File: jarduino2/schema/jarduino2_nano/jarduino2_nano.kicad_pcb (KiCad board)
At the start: 2 copper layers, 118 x 95 mm, 38 parts, among them J1 Power, J2 Interface, J3 Pompe 1, J4 Pompe 2, Q1 Q_NPN_BCE, Q2 Q_NPN_BCE, U1 RFB-0505S, U2 RtcArduino

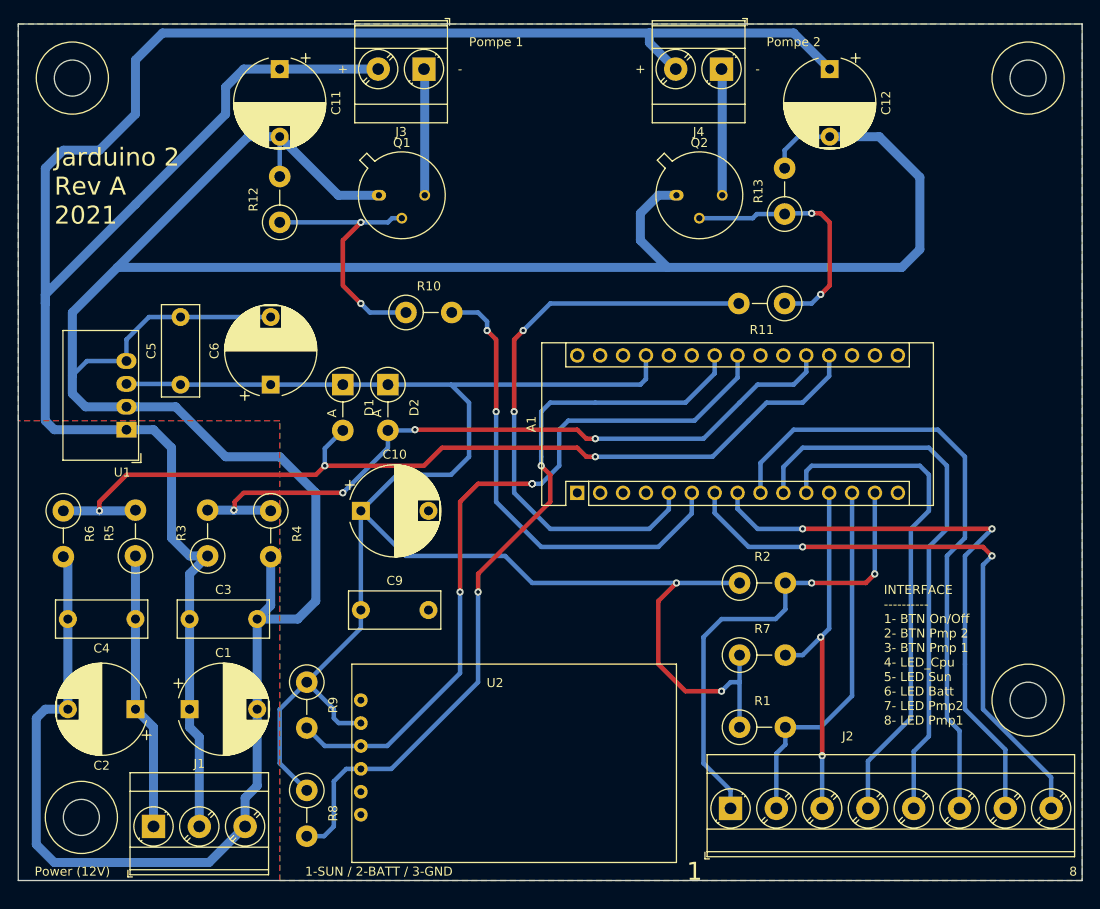
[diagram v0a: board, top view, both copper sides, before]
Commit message: Ajout capteur de temp et hum + ext serie
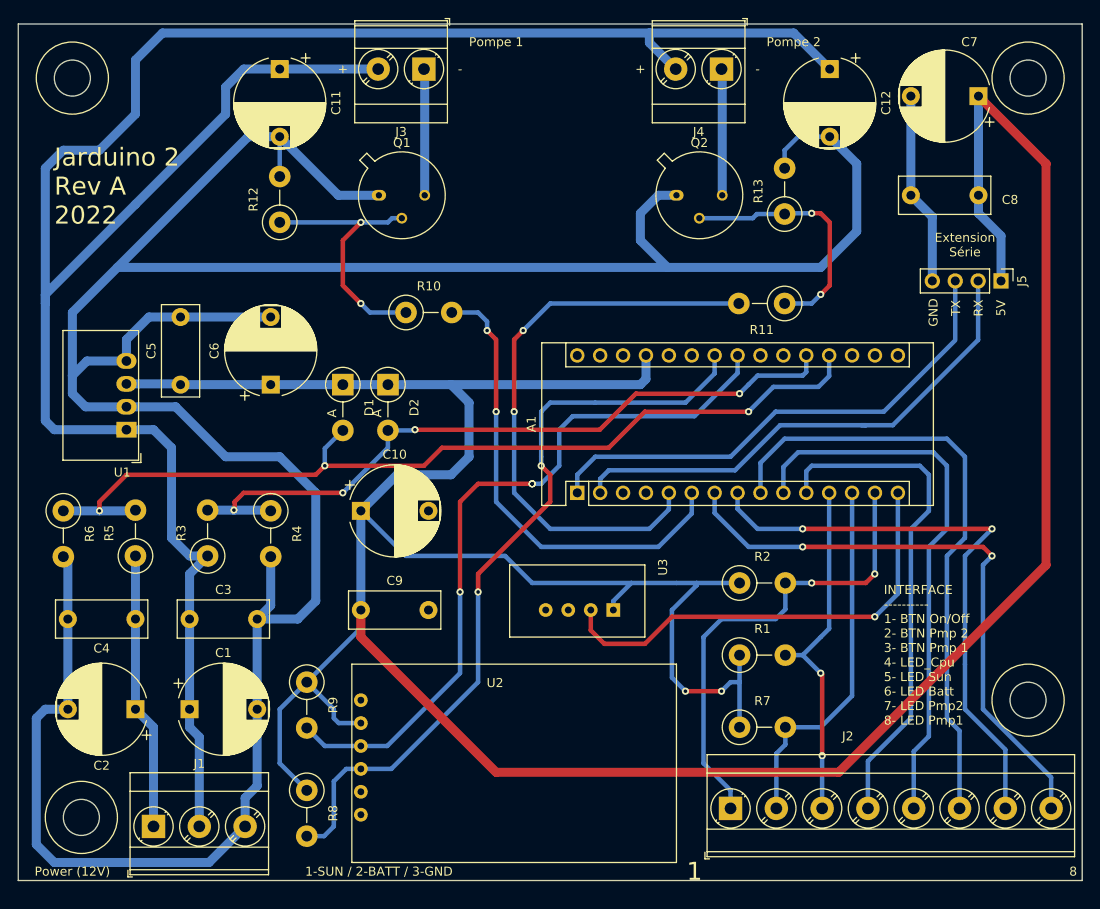
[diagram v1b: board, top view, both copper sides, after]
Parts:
- added C7: 50µF / 50V, Capacitor_THT:CP_Radial_D10.0mm_P7.50mm, F.Cu at (172.5, 52.0)
- added C8: 1nF / 50V, Capacitor_THT:C_Rect_L10.0mm_W4.0mm_P7.50mm_MKS4, F.Cu at (172.5, 63.0)
- added J5: Ext Ser, Connector_PinHeader_2.54mm:PinHeader_1x04_P2.54mm_Vertical, F.Cu at (175.0, 72.5)
- added U3: DHT22, bpc:BPC_DHT22, F.Cu at (132.0, 109.0)
- A1: footprint bpc:BPC_Arduino_Nano -> Module:Arduino_Nano
- R1, R2, R3, R5, R7: value R -> 100k
- R4, R6: value R -> 40k
- R8, R9: value R -> 10k
- moved R1 8.00 mm to (146.0, 114.0)
- moved R7 8.00 mm to (146.0, 122.0)
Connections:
- R1 pad 2: BTN_PMP2 -> BTN_PMP1
- R7 pad 2: BTN_PMP1 -> BTN_PMP2
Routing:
- net +5V: track 202.1 -> 381.0 mm
- net Net-(A1-Pad2): track 0.00 -> 56.9 mm
- net Net-(A1-Pad1): track 0.00 -> 56.5 mm
- net Net-(A1-Pad15): track 0.00 -> 50.4 mm, vias 0 -> 1
- net GND: track 356.3 -> 363.5 mm
- net BTN_PMP1: track 40.2 -> 39.0 mm
- net POW_SUN: track 103.6 -> 102.8 mm
- net POW_BATT: track 81.3 -> 80.4 mm
- net LED_12V_BATT: track 69.2 -> 68.3 mm
- removed copper zone on B.Cu, net GND
- removed copper zone on F.Cu, net GND
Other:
- board text added: "5V"
- board text added: "Extension Série"
- board text added: "GND"
- board text added: "Jarduino 2 Rev A 2022"
- board text added: "RX"
- board text added: "TX"
- board text removed: "Jarduino 2 Rev A 2021"

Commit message: Amélioration 3d / libs
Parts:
- A1: footprint Module:Arduino_Nano -> bpc:BPC_Arduino_Nano
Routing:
- added copper zone on B.Cu, net GND
